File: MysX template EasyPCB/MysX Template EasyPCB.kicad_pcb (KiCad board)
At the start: 2 copper layers, 50.2 x 50.2 mm, 1 part, among them P2 MYSX_2.4

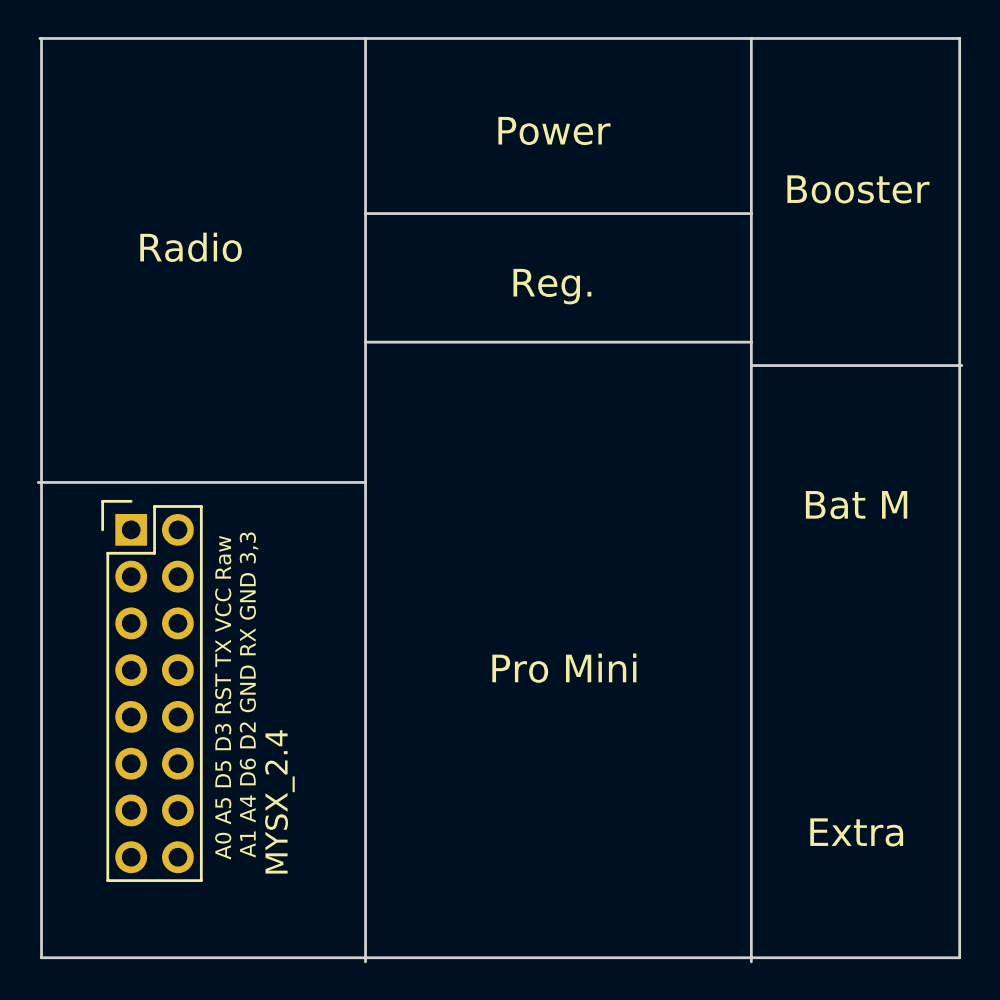
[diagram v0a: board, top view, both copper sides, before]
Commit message: Added mounting holes
M Hole
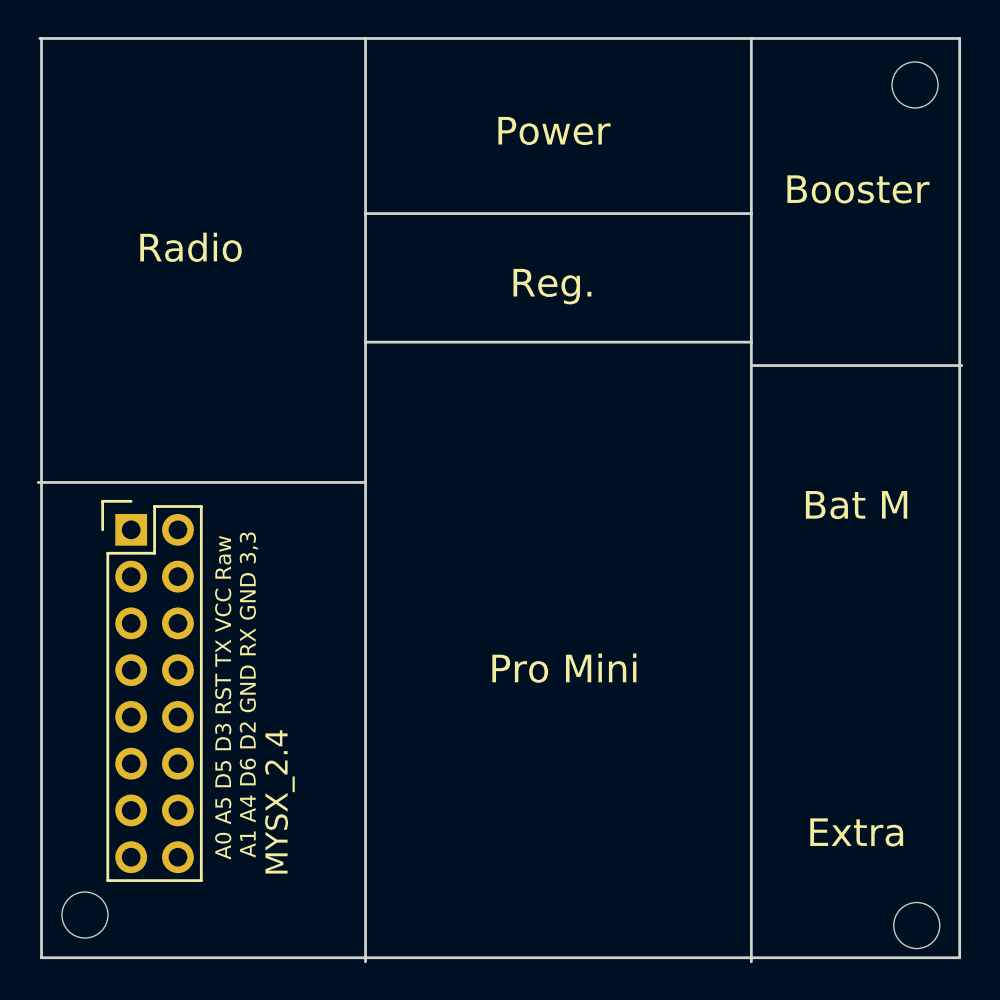
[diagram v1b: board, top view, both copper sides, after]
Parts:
- added REF**: MountingHole_2.5mm, Mounting_Holes:MountingHole_2.5mm, F.Cu at (172.1, 64.1)
- added REF**: MountingHole_2.5mm, Mounting_Holes:MountingHole_2.5mm, F.Cu at (172.2, 109.8)
- added REF**: MountingHole_2.5mm, Mounting_Holes:MountingHole_2.5mm, F.Cu at (127.0, 109.2)
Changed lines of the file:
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@@
 (kicad_pcb (version 4) (host pcbnew 4.0.4-stable)
   (general
-    (links 2)
+    (links 0)
     (no_connects 2)
-    (area 124.384999 61.519999 174.700001 111.835001)
+    (area 118.771429 59.25 180.408572 116.045)
     (thickness 1.6)
     (drawings 21)
     (tracks 0)
     (zones 0)
-    (modules 1)
+    (modules 4)
     (nets 3)
   )
@@
     (uvia_drill 0.1)
   )
+  (module Mounting_Holes:MountingHole_2.5mm (layer F.Cu)
+    (at 172.085 64.135)
+    (descr "Mounting Hole 2.5mm, no annular")
+    (tags "mounting hole 2.5mm no annular")
+    (attr virtual)
+    (fp_text reference REF** (at 0 -3.81) (layer F.SilkS) hide
+      (effects (font (size 1 1) (thickness 0.15)))
+    )
+    (fp_text value MountingHole_2.5mm (at 0 -3.81) (layer F.Fab) hide
+      (effects (font (size 1 1) (thickness 0.15)))
+    )
+    (fp_text user %R (at 1.27 -3.81) (layer F.Fab) hide
+      (effects (font (size 1 1) (thickness 0.15)))
+    )
+    (fp_circle (center 0 0) (end 2.5 0) (layer Cmts.User) (width 0.15))
+    (fp_circle (center 0 0) (end 2.75 0) (layer F.CrtYd) (width 0.05))
+    (pad 1 np_thru_hole circle (at 0 0) (size 2.5 2.5) (drill 2.5) (layers *.Cu *.Mask))
+  )
+  (module Mounting_Holes:MountingHole_2.5mm (layer F.Cu)
+    (at 172.18 109.79)
+    (descr "Mounting Hole 2.5mm, no annular")
+    (tags "mounting hole 2.5mm no annular")
+    (attr virtual)
+    (fp_text reference REF** (at -4.445 5.08) (layer F.SilkS) hide
+      (effects (font (size 1 1) (thickness 0.15)))
+    )
+    (fp_text value MountingHole_2.5mm (at 0 3.5) (layer F.Fab) hide
+      (effects (font (size 1 1) (thickness 0.15)))
+    )
+    (fp_text user %R (at -0.635 5.08) (layer F.Fab) hide
+      (effects (font (size 1 1) (thickness 0.15)))
+    )
+    (fp_circle (center 0 0) (end 2.5 0) (layer Cmts.User) (width 0.15))
+    (fp_circle (center 0 0) (end 2.75 0) (layer F.CrtYd) (width 0.05))
+    (pad 1 np_thru_hole circle (at 0 0) (size 2.5 2.5) (drill 2.5) (layers *.Cu *.Mask))
+  )
   (module mysensors_connectors:MYSX_2.4 locked (layer F.Cu)
     (at 129.51 88.3)
@@
     )
   )
+  (module Mounting_Holes:MountingHole_2.5mm (layer F.Cu)
+    (at 127 109.22)
+    (descr "Mounting Hole 2.5mm, no annular")
+    (tags "mounting hole 2.5mm no annular")
+    (attr virtual)
+    (fp_text reference REF** (at -4.445 5.08) (layer F.SilkS) hide
+      (effects (font (size 1 1) (thickness 0.15)))
+    )
+    (fp_text value MountingHole_2.5mm (at 0 3.5) (layer F.Fab) hide
+      (effects (font (size 1 1) (thickness 0.15)))
+    )
+    (fp_text user %R (at -0.635 5.08) (layer F.Fab) hide
+      (effects (font (size 1 1) (thickness 0.15)))
+    )
+    (fp_circle (center 0 0) (end 2.5 0) (layer Cmts.User) (width 0.15))
+    (fp_circle (center 0 0) (end 2.75 0) (layer F.CrtYd) (width 0.05))
+    (pad 1 np_thru_hole circle (at 0 0) (size 2.5 2.5) (drill 2.5) (layers *.Cu *.Mask))
+  )
   (gr_text Booster (at 168.91 69.85) (layer F.SilkS)
